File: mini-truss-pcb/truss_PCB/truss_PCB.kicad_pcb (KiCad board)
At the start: 2 copper layers, 114.3 x 102.9 mm, 208 parts, among them IC1 BAJ0BC0FP-E2, J1 XT60_60A_male, J10 IN_B, J11 IN_B, J12 Serial IO, J13 IO Header, J14 LV IO, J15 HV IO, J16 GND, J17 GND, J18 12V, J19 6V, J2 LimitSwitch, J20 5V, J21 3V3, J22 10V, J3 Servo, J4 Truss Connection, J5 IN_B, J6 IN_B, J7 IN_B, J8 IN_B, J9 IN_B, Q1 BC807, Q2 BC807, Q3 BC807, Q4 BC807, Q5 BC807, Q6 BC807, Q7 BC807, Q8 IRF5305_PBF, U1 HX711, U11 LM2596S-ADJ, U12 AMS1117-5.0, U13 AMS1117-3.3, U2 HX711, U3 HX711, U4 HX711, U5 HX711, U6 HX711, U7 HX711, U8 TXS0108EPW, U9 TXS0108EPW

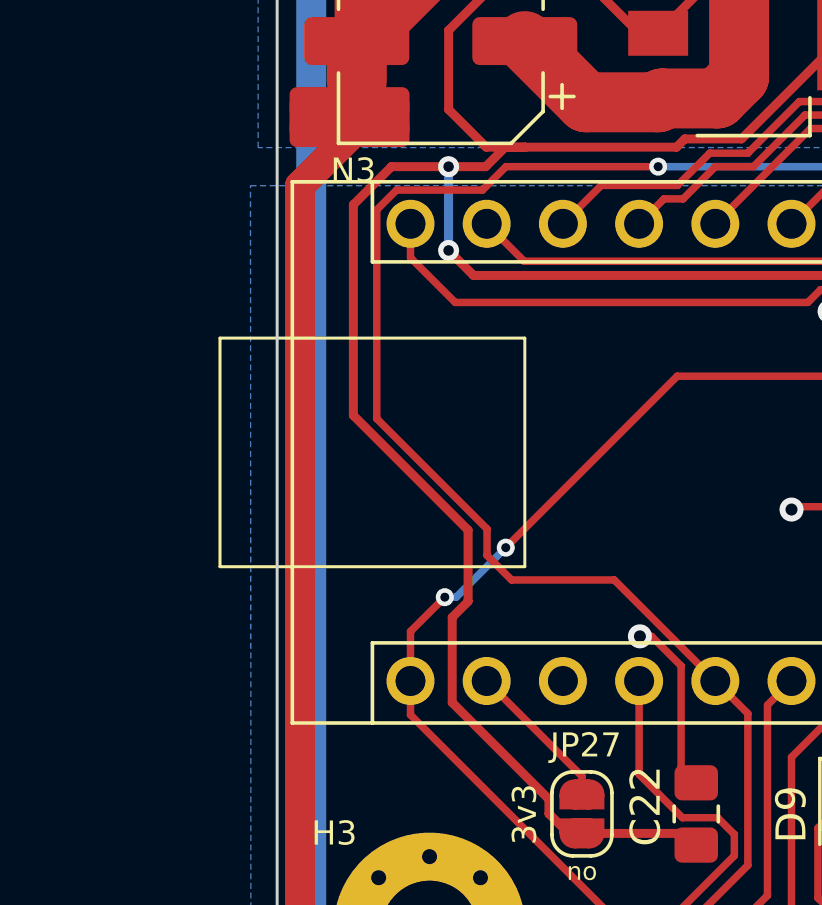
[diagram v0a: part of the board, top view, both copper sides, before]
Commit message: added basic firmware tests
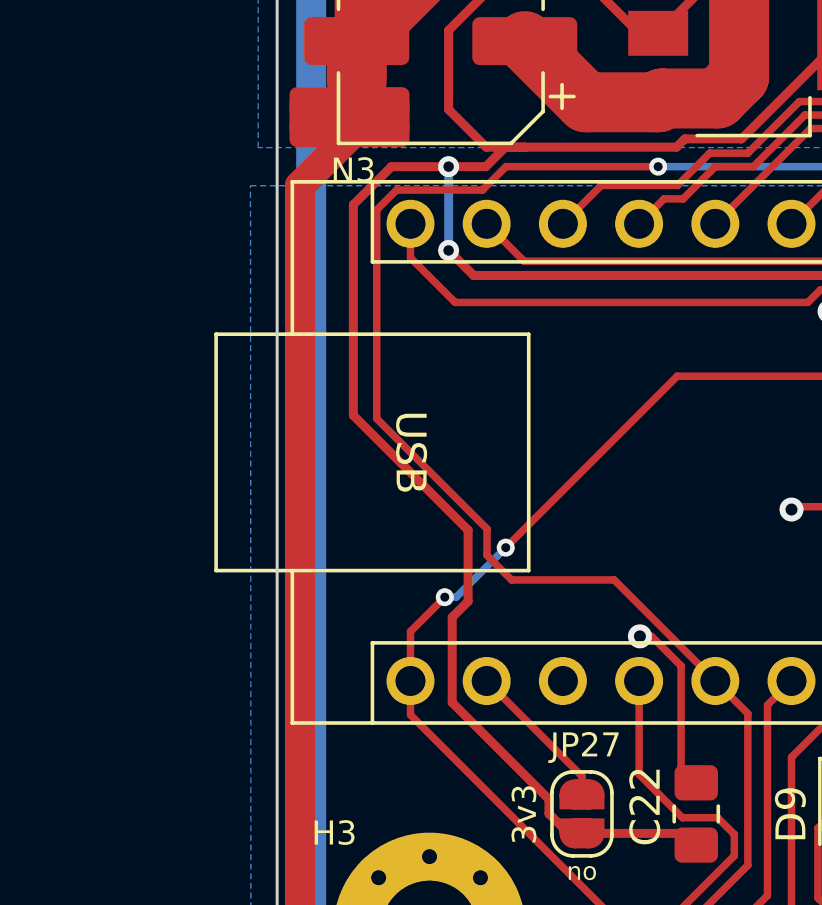
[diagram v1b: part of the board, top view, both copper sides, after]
